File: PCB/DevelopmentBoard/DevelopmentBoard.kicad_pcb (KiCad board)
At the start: 2 copper layers, 128.3 x 64.8 mm, 37 parts, among them IC1 FE1.1S_USB_Controller, J1 Conn_01x04_MountingPin, J2 USB-A, J3 USB-A, J4 CRJ007_RJ45, U1 Pi_CM4, U2 Barometer_Grove, U3 D24V22F5, U4 Micro-USB, U5 VN-100_Breakout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

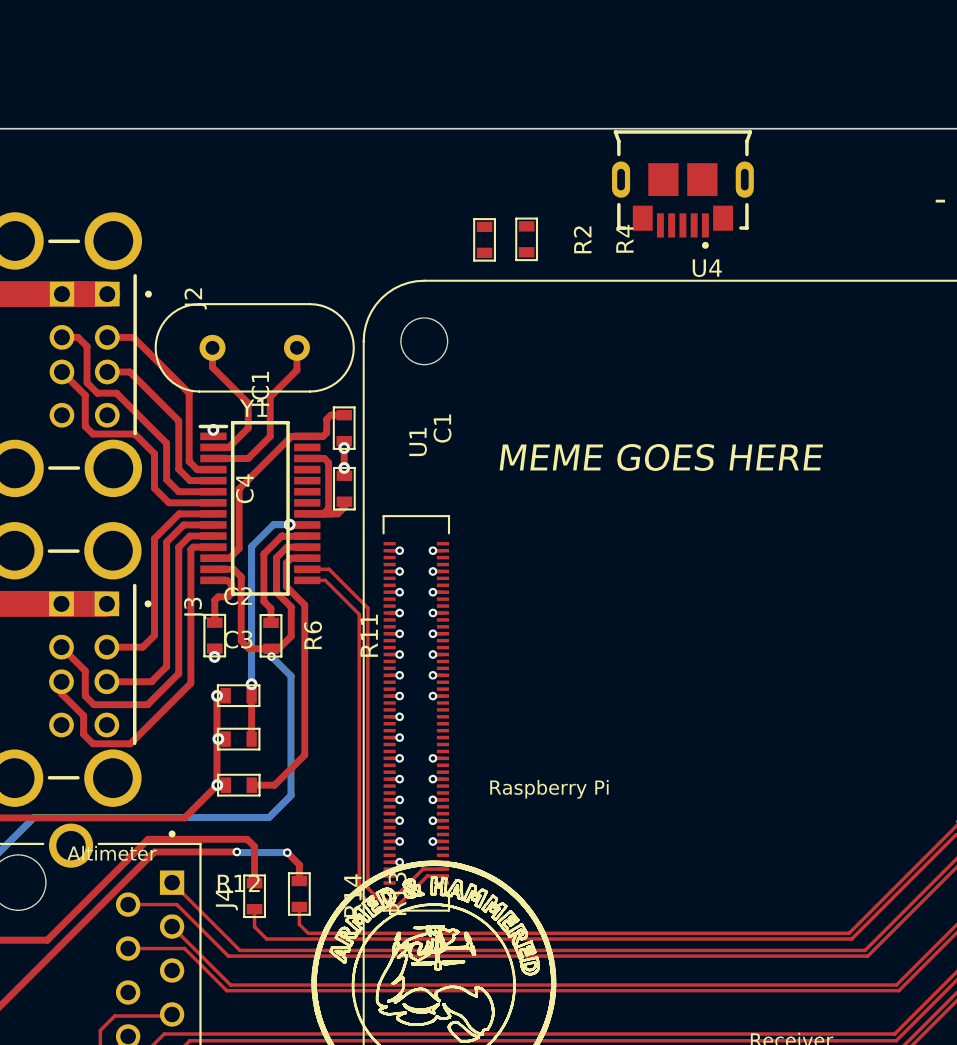
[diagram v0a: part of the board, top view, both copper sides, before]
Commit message: Moved USB Jumper/0hm resistors
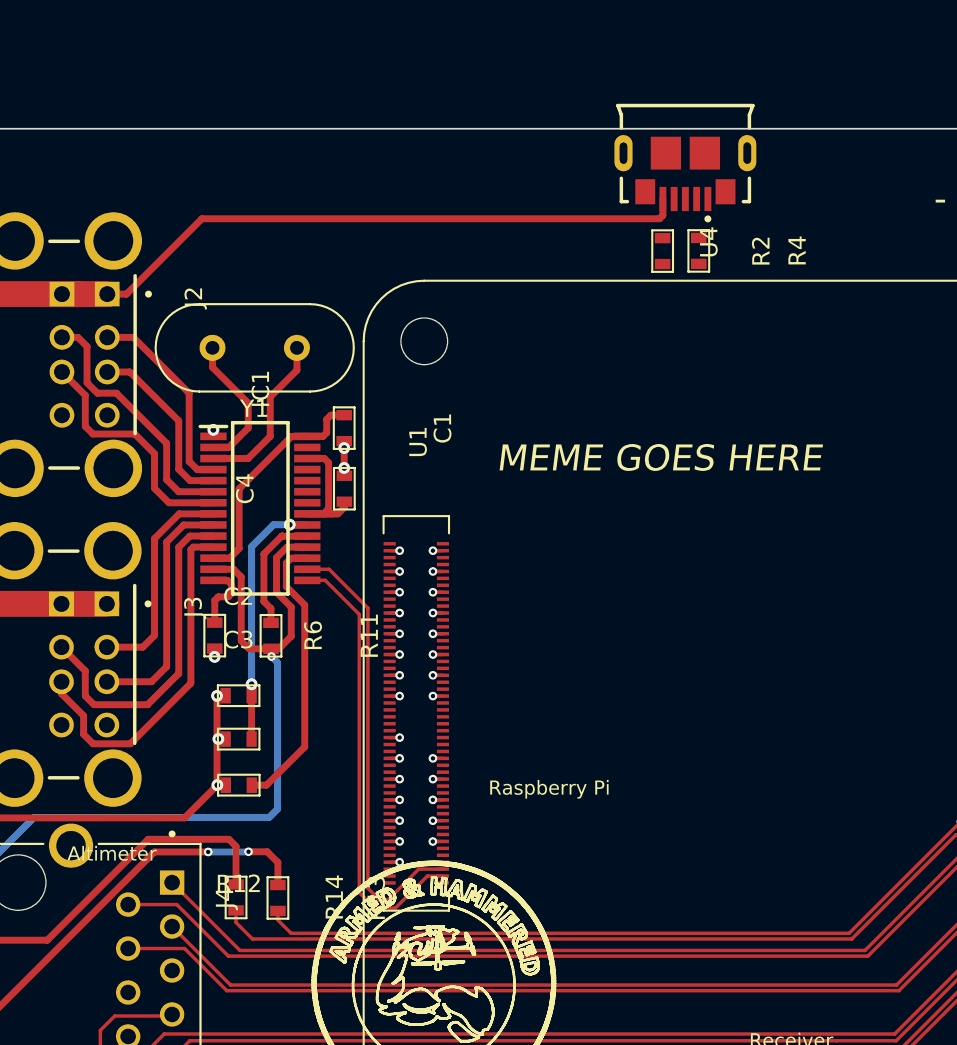
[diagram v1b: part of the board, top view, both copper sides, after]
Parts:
- moved R2 10.3 mm to (137.7, 72.9)
- moved R4 9.97 mm to (139.8, 72.8)
- moved U4 1.53 mm to (140.4, 69.8)
- moved R13 1.26 mm to (115.5, 110.2)
- moved R14 1.07 mm to (113.1, 110.2)
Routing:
- net +5V: track 354.4 -> 389.3 mm
- net Net-(J4-Pad12): track 23.1 -> 22.1 mm
- net Net-(J4-Pad13): track 26.3 -> 25.4 mm
- net /ETH_LEDG: track 46.3 -> 47.1 mm
- net /ETH_LEDY: track 48.7 -> 49.5 mm
- net +3V3: track 90.7 -> 90.0 mm
- net GND: track 29.4 -> 28.8 mm, vias 49 -> 48

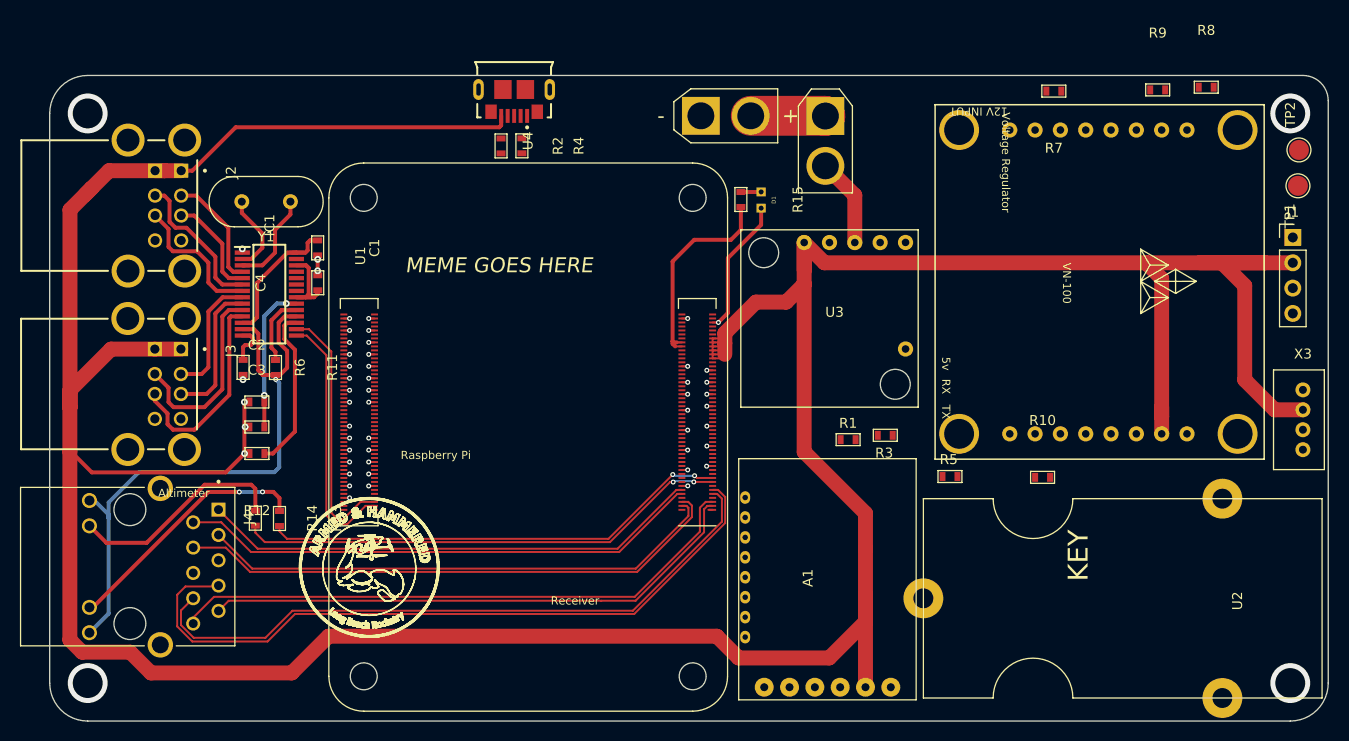
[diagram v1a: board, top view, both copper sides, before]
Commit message: Routed traces from VN-100 breakout
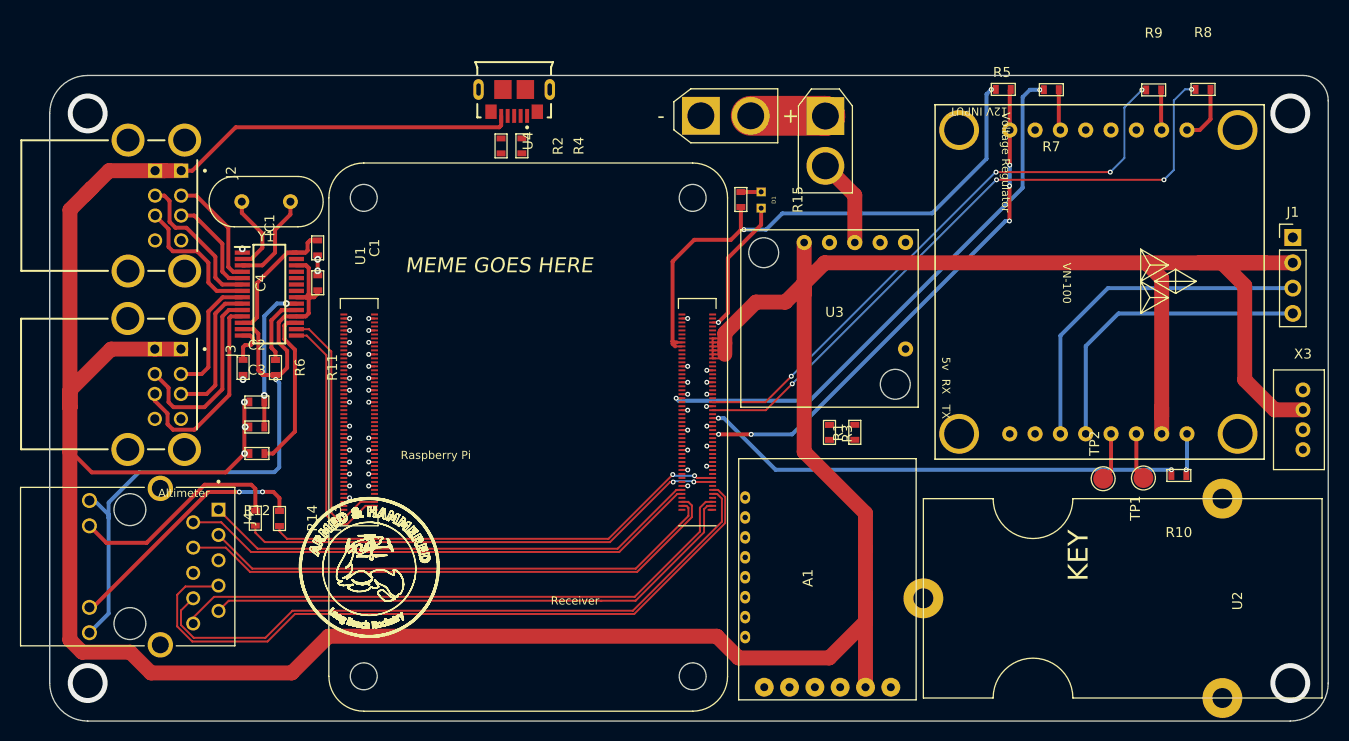
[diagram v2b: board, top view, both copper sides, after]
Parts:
- moved R5 39.2 mm to (188.1, 67.2)
- moved TP2 38.4 mm to (198.1, 106.2)
- moved TP1 33.2 mm to (202.2, 106.2)
- moved R10 13.7 mm to (205.7, 105.9), turned to 180 degrees
- moved R3 5.61 mm to (170.7, 101.6), turned to 90 degrees
- moved R1 1.00 mm to (173.2, 101.6), turned to 90 degrees
- moved R9 0.40 mm to (203.2, 67.2)
- moved R8 0.39 mm to (208.2, 67.2)
- moved R7 0.29 mm to (192.9, 67.2)
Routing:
- net /RX: track 0.00 -> 65.9 mm, vias 0 -> 4
- net /TX: track 0.00 -> 59.5 mm, vias 0 -> 4
- net /MCU_Reset: track 0.00 -> 55.8 mm, vias 0 -> 2
- net /VN-100_CS: track 0.00 -> 51.9 mm, vias 0 -> 5
- net /VN-100_Enable: track 0.00 -> 48.8 mm, vias 0 -> 2
- net +3V3: track 90.0 -> 128.5 mm, vias 1 -> 3
- net Net-(J1-Pad3): track 0.00 -> 35.1 mm
- net Net-(J1-Pad4): track 0.00 -> 30.9 mm
- net Net-(R8-Pad2): track 0.00 -> 5.80 mm
- net Net-(TP2-Pad1): track 0.00 -> 4.83 mm
- net Net-(TP1-Pad1): track 0.00 -> 4.72 mm
- net Net-(R10-Pad1): track 0.00 -> 4.33 mm, vias 0 -> 1
- net Net-(R7-Pad1): track 0.00 -> 4.11 mm
- net Net-(R9-Pad2): track 0.00 -> 4.05 mm
- net +5V: track 389.3 -> 387.6 mm

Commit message: Routed I2C traces
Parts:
- moved R1 41.1 mm to (148.2, 69.0)
- moved R3 38.4 mm to (150.5, 68.9)
- moved R2 1.02 mm to (137.5, 71.9), turned to 0 degrees
- moved R4 1.01 mm to (140.1, 71.9), turned to 180 degrees
- moved R10 1.00 mm to (205.8, 106.9)
- moved TP2 0.90 mm to (198.6, 107.0)
- moved TP1 0.65 mm to (202.2, 106.8)
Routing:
- net /SDA: track 0.00 -> 81.8 mm, vias 0 -> 1
- net /SCL: track 0.00 -> 75.4 mm, vias 0 -> 1
- net +5V: track 387.6 -> 316.8 mm
- net /VN-100_MOSI: track 0.00 -> 53.7 mm, vias 0 -> 8
- net /CH1: track 0.00 -> 30.9 mm, vias 0 -> 3
- net /VN-100_SCK: track 0.00 -> 30.0 mm, vias 0 -> 4
- net /CH2: track 0.00 -> 29.4 mm, vias 0 -> 3
- net /VN-100_MISO: track 0.00 -> 27.6 mm, vias 0 -> 4
- net /SBUS: track 0.00 -> 16.6 mm, vias 0 -> 2
- net /VN-100_Enable: track 48.8 -> 55.4 mm, vias 2 -> 4
- net /MCU_Reset: track 55.8 -> 60.1 mm, vias 2 -> 8
- net Net-(J1-Pad3): track 35.1 -> 31.8 mm, vias 0 -> 4
- net GND: track 28.9 -> 25.9 mm, vias 48 -> 40
- net Net-(J1-Pad4): track 30.9 -> 28.4 mm, vias 0 -> 4
- net /TX: track 59.5 -> 62.0 mm
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
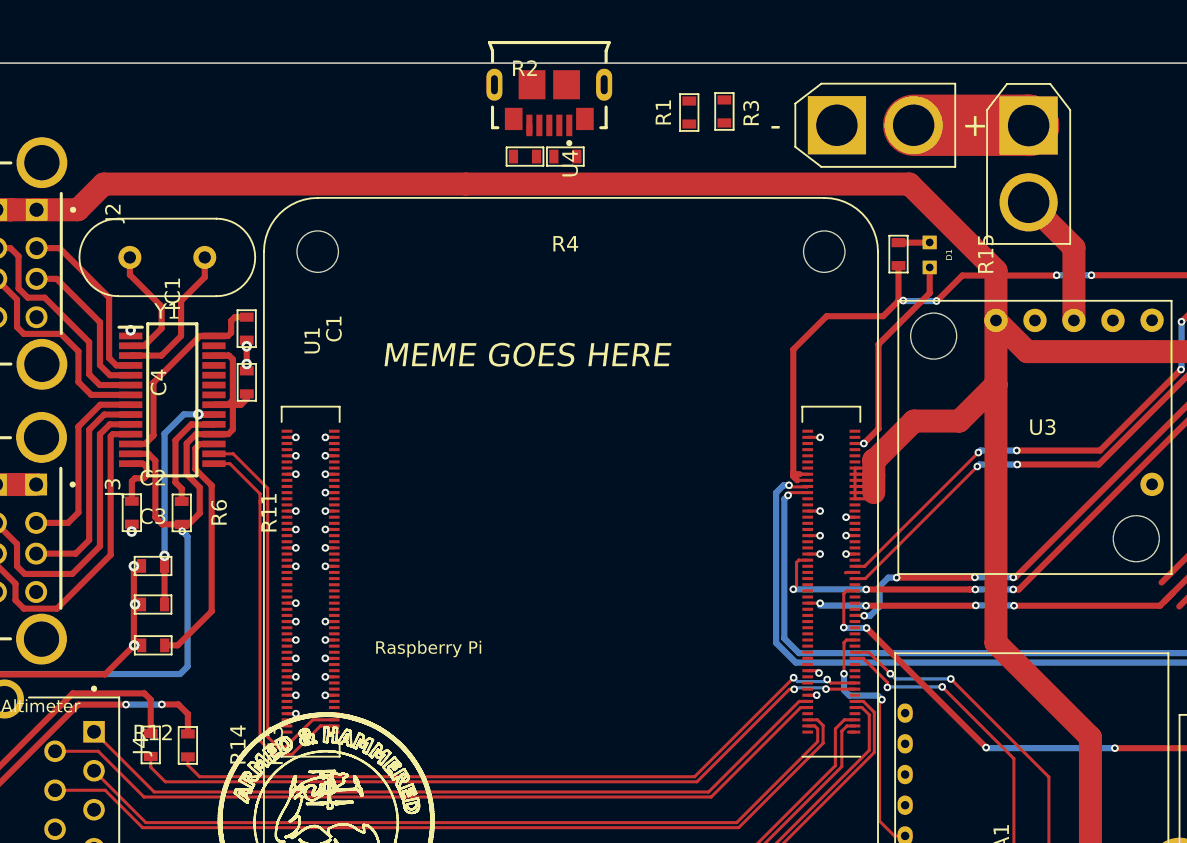
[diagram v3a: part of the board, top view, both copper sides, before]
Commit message: Set I2C pullups
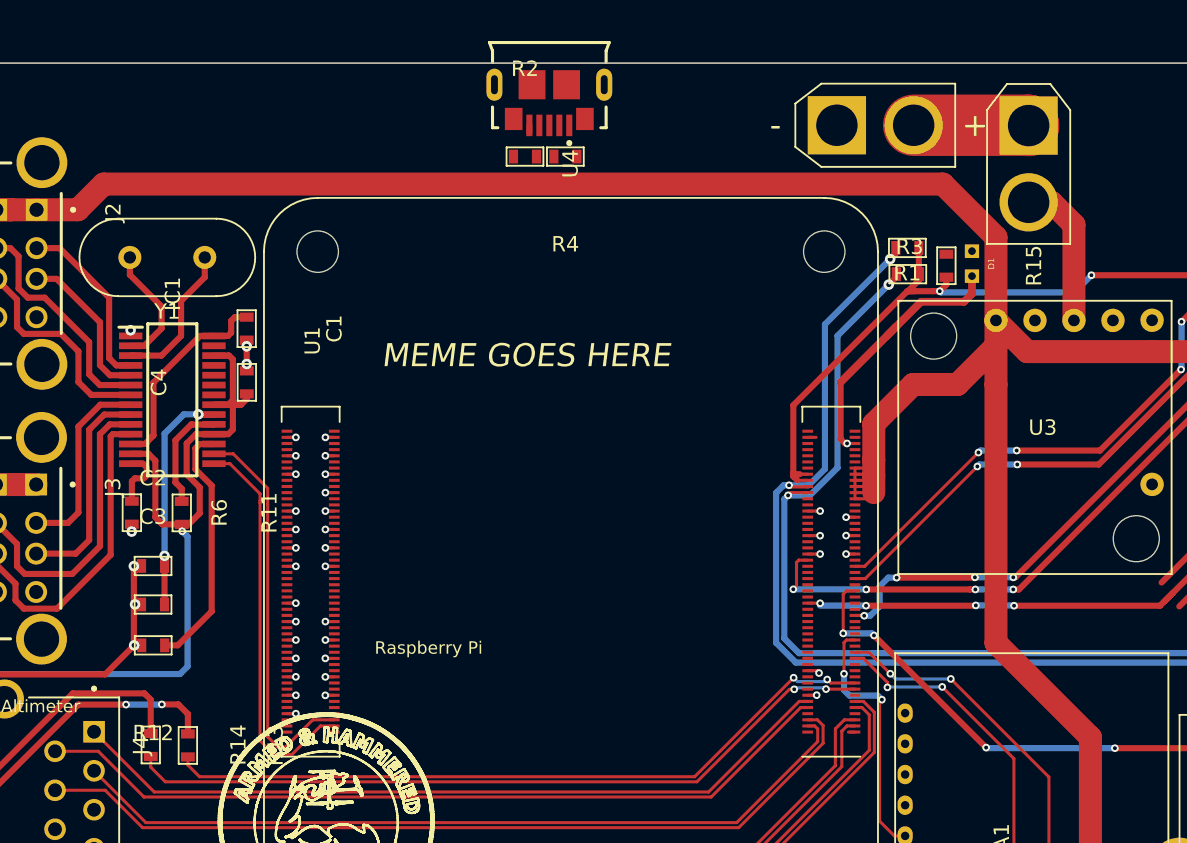
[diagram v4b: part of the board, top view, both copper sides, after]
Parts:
- moved R1 16.7 mm to (162.4, 77.8), turned to 180 degrees
- moved R3 16.0 mm to (162.4, 79.5), turned to 180 degrees
- moved R15 3.21 mm to (164.9, 79.0)
- moved D1 2.81 mm to (166.6, 78.8)
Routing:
- net /SDA: track 81.8 -> 100.9 mm, vias 1 -> 2
- net /SCL: track 75.4 -> 93.5 mm, vias 1 -> 2
- net Net-(D1-Pad1): track 13.8 -> 17.7 mm
- net +5V: track 316.8 -> 320.5 mm
- net Net-(D1-Pad2): track 2.04 -> 0.00 mm
- net GND: track 25.9 -> 25.0 mm, vias 40 -> 39
- net Net-(U3-Pad3): track 8.92 -> 9.79 mm
- net +3V3: track 128.7 -> 129.1 mm, vias 5 -> 3

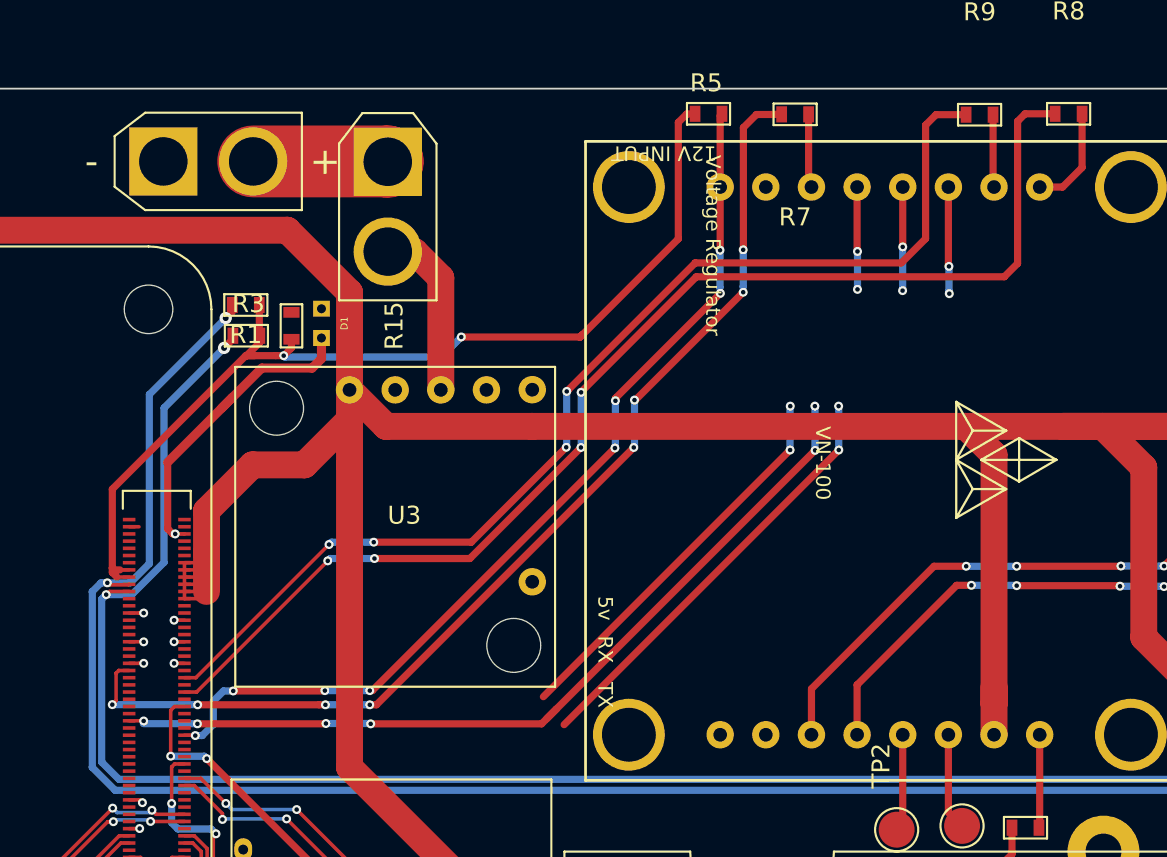
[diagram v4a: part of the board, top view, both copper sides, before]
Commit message: Rerouted UART and SPI traces
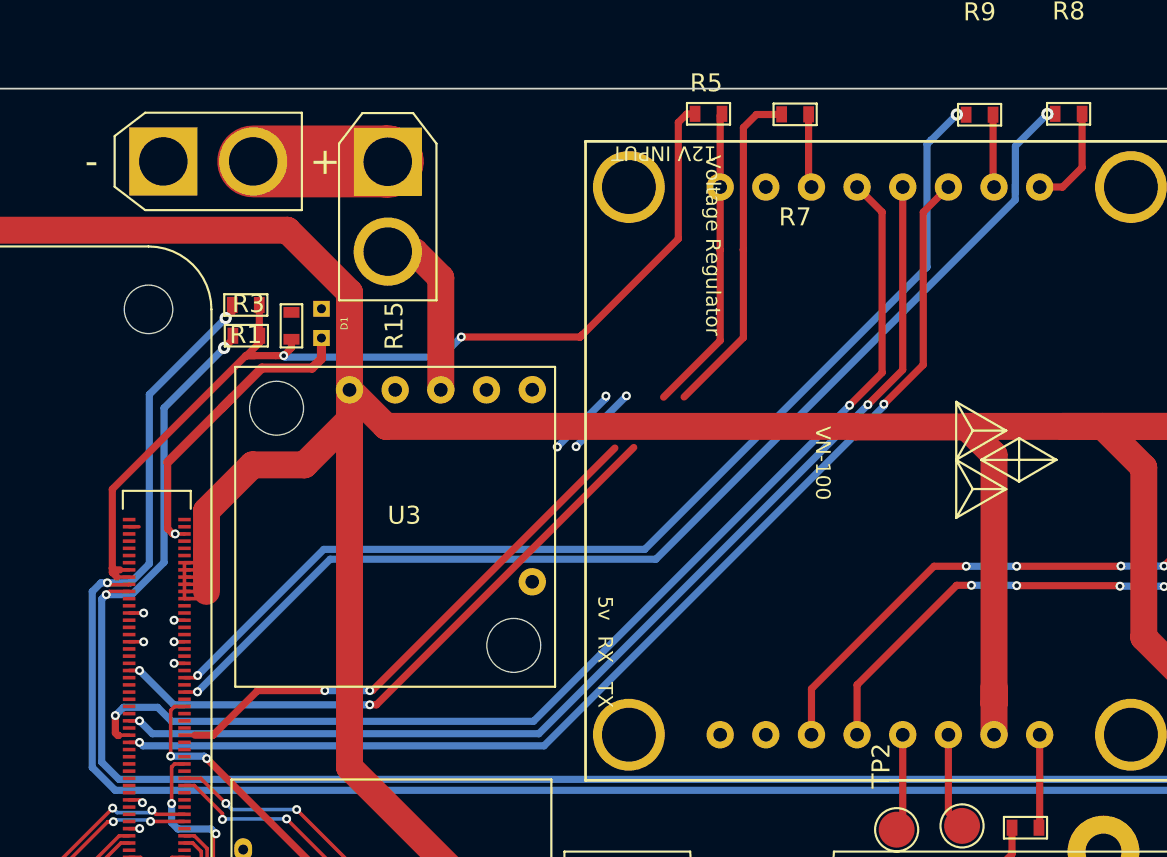
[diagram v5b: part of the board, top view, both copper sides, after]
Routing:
- net /VN-100_MISO: track 27.6 -> 63.9 mm, vias 4 -> 2
- net /VN-100_SCK: track 30.0 -> 63.6 mm, vias 4 -> 2
- net /VN-100_MOSI: track 53.7 -> 61.9 mm, vias 8 -> 2
- net /RX: track 68.2 -> 64.0 mm, vias 4 -> 2
- net /MCU_Reset: track 60.1 -> 57.7 mm, vias 8 -> 4
- net /TX: track 62.0 -> 60.5 mm, vias 4 -> 2
- net GND: track 25.0 -> 24.2 mm, vias 39 -> 38
- net /VN-100_CS: track 52.1 -> 51.7 mm, vias 8 -> 4
